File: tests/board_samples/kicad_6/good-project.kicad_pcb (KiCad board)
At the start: 6 copper layers, 45.7 x 21.6 mm, 4 parts, among them P1 CONN_01X02

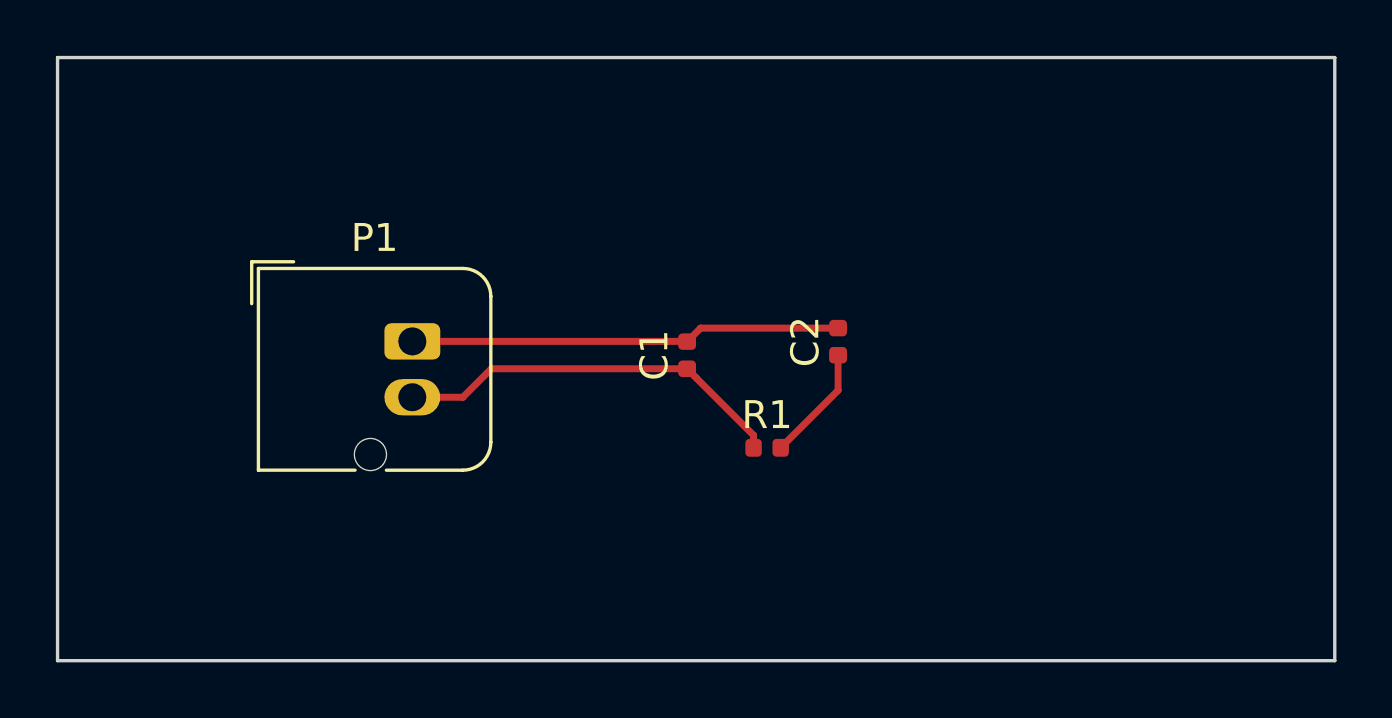
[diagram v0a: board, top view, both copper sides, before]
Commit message: Updated v6 version of good-project (HPGL pen diameter changed)
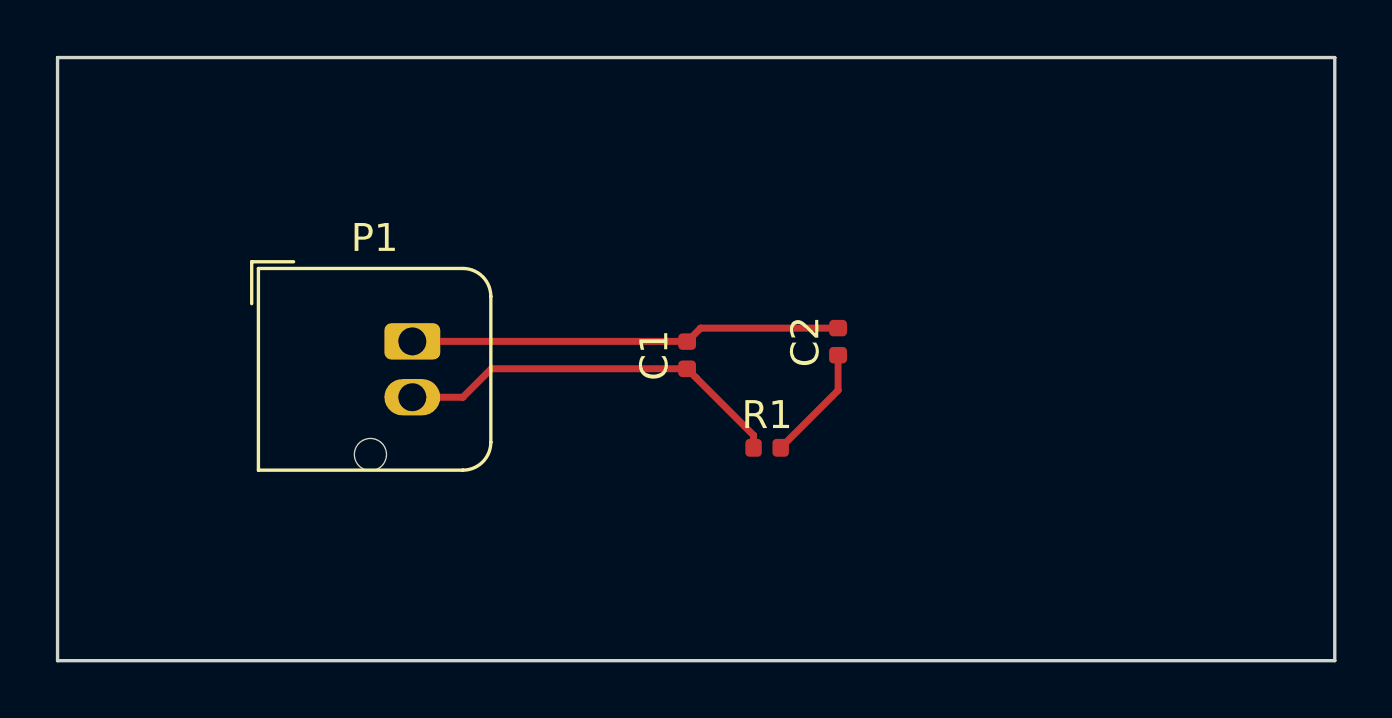
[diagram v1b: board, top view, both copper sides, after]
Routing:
- net /Power/VCC: track 157.2 -> 14.1 mm
- net GND: track 158.6 -> 15.4 mm
- net (no net): track 0.00 -> 132.0 mm
